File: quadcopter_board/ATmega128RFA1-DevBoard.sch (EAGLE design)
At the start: 75 parts, among them J1 ISP, Q1 CJ2302, Q2 CJ2302, Q3 CJ2302, Q4 CJ2302, U1 ATMEGA128RFA1

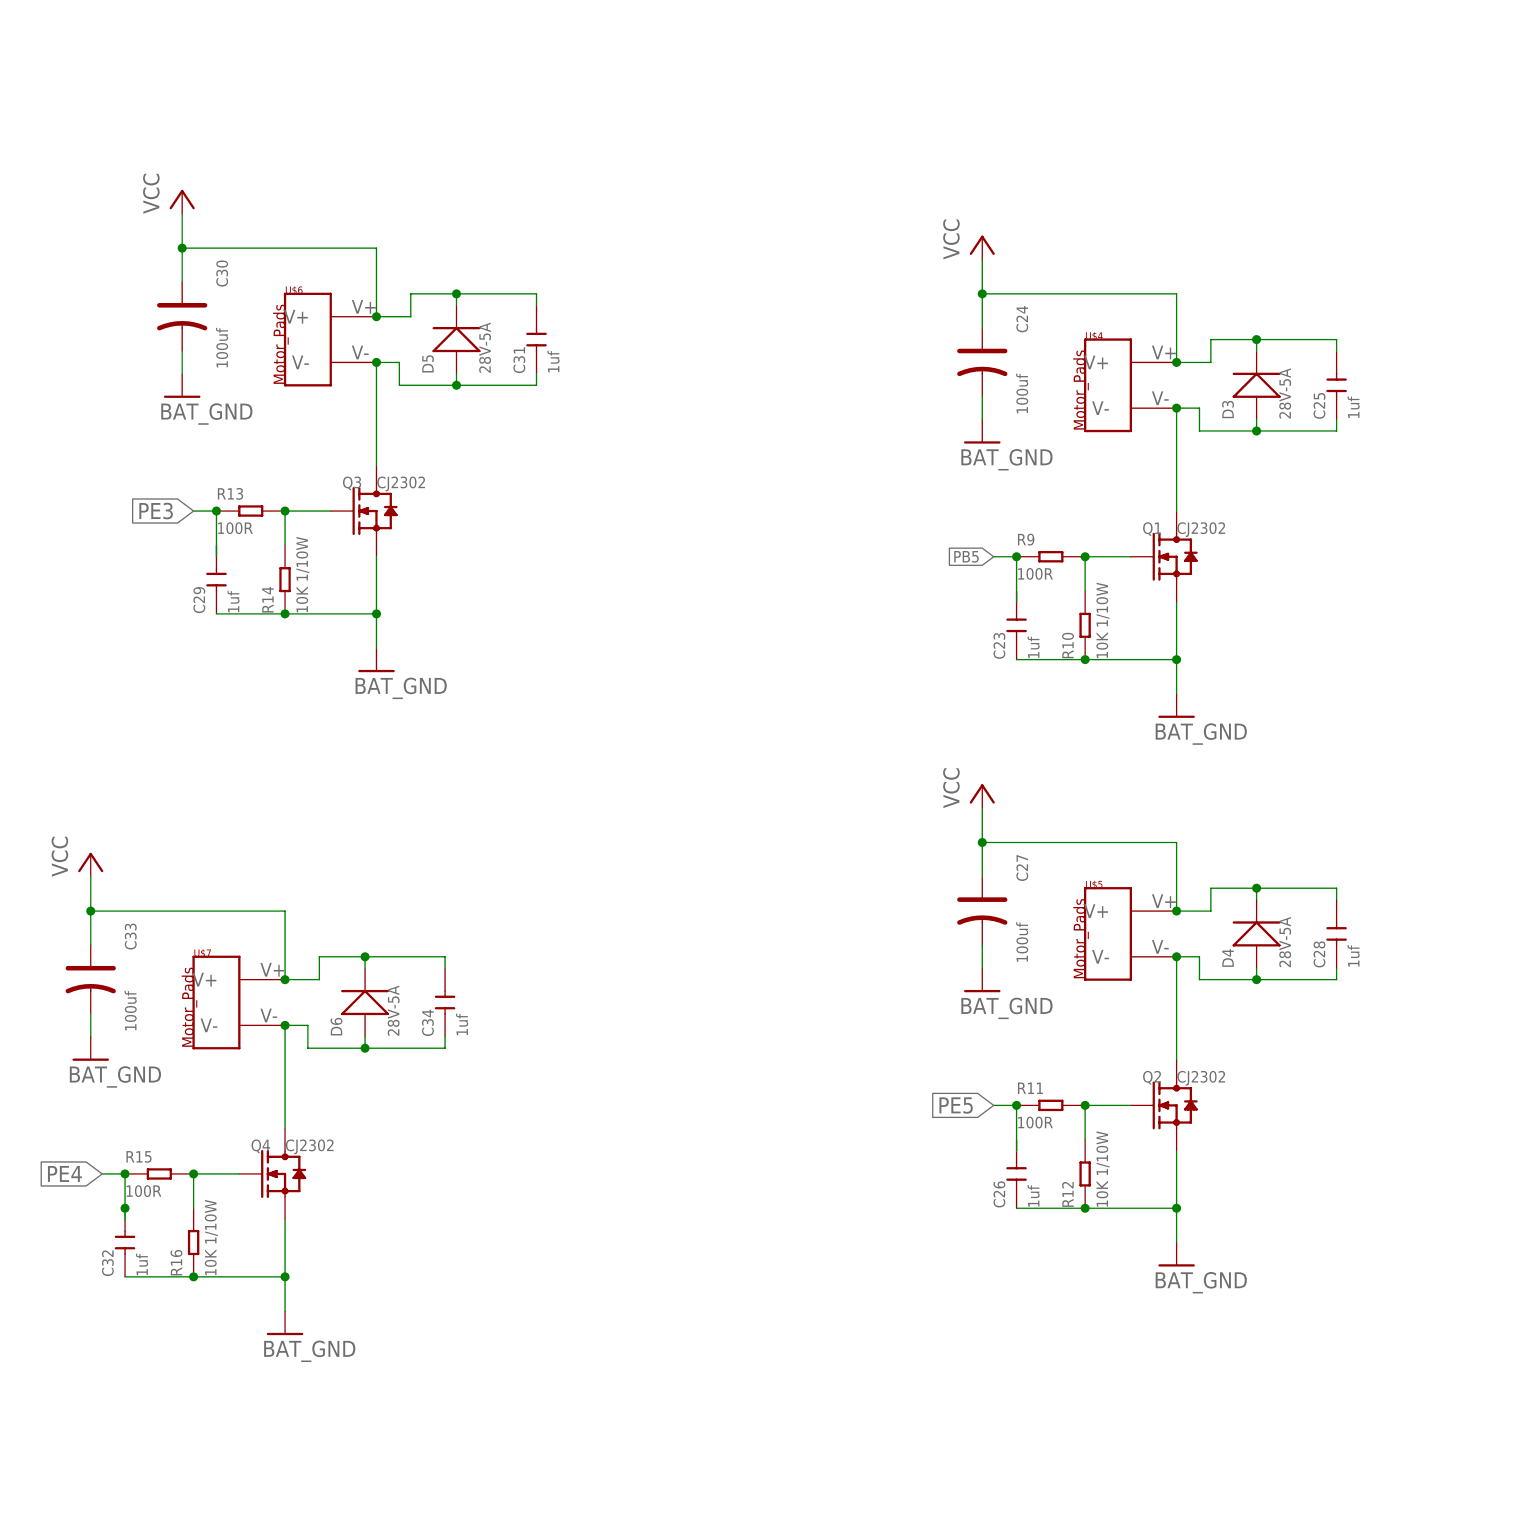
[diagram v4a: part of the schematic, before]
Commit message: clear up of motor driver layout
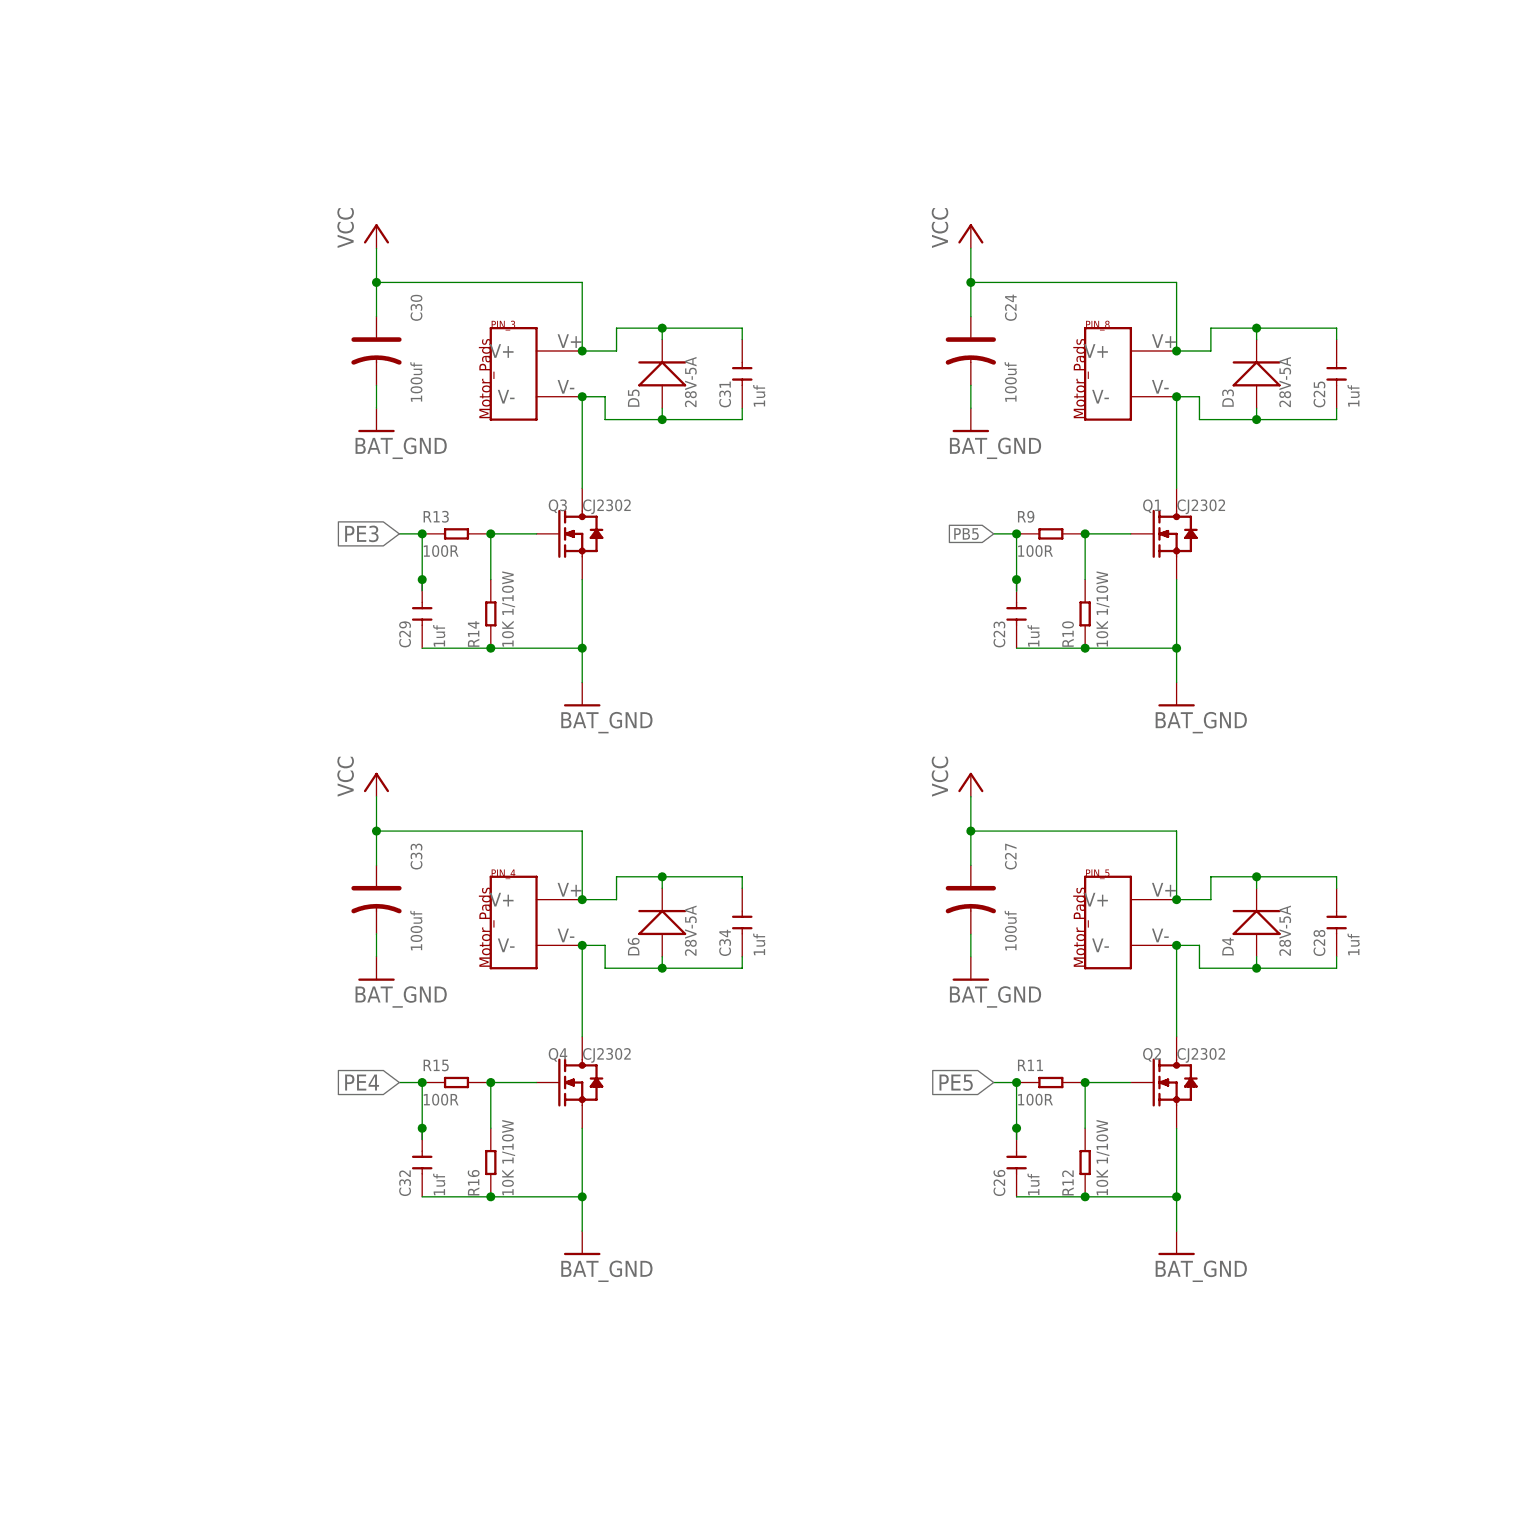
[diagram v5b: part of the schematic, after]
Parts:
- removed U$4, U$5, U$6, U$7: MOTOR_PADS, Andranik-Lab4:MOTOR_PADS
- added PIN_3, PIN_4, PIN_5, PIN_8: MOTOR_PADS, Andranik-Lab4:MOTOR_PADS
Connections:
- net N$19: now also PIN_8.V-; no longer U$4.V-
- net N$22: now also PIN_5.V-; no longer U$5.V-
- net N$25: now also PIN_3.V-; no longer U$6.V-
- net N$28: now also PIN_4.V-; no longer U$7.V-
- net PB5: now also C23.2
- net PE3: now also C29.2
- net PE5: now also C26.2
- net VCC: now also PIN_3.V+, PIN_4.V+, PIN_5.V+, PIN_8.V+; no longer U$4.V+, U$5.V+, U$6.V+, U$7.V+
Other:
- moved on the sheet: C23, C24, C25, C26, C27, C28, C29, C30, C31, C32, C33, C34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

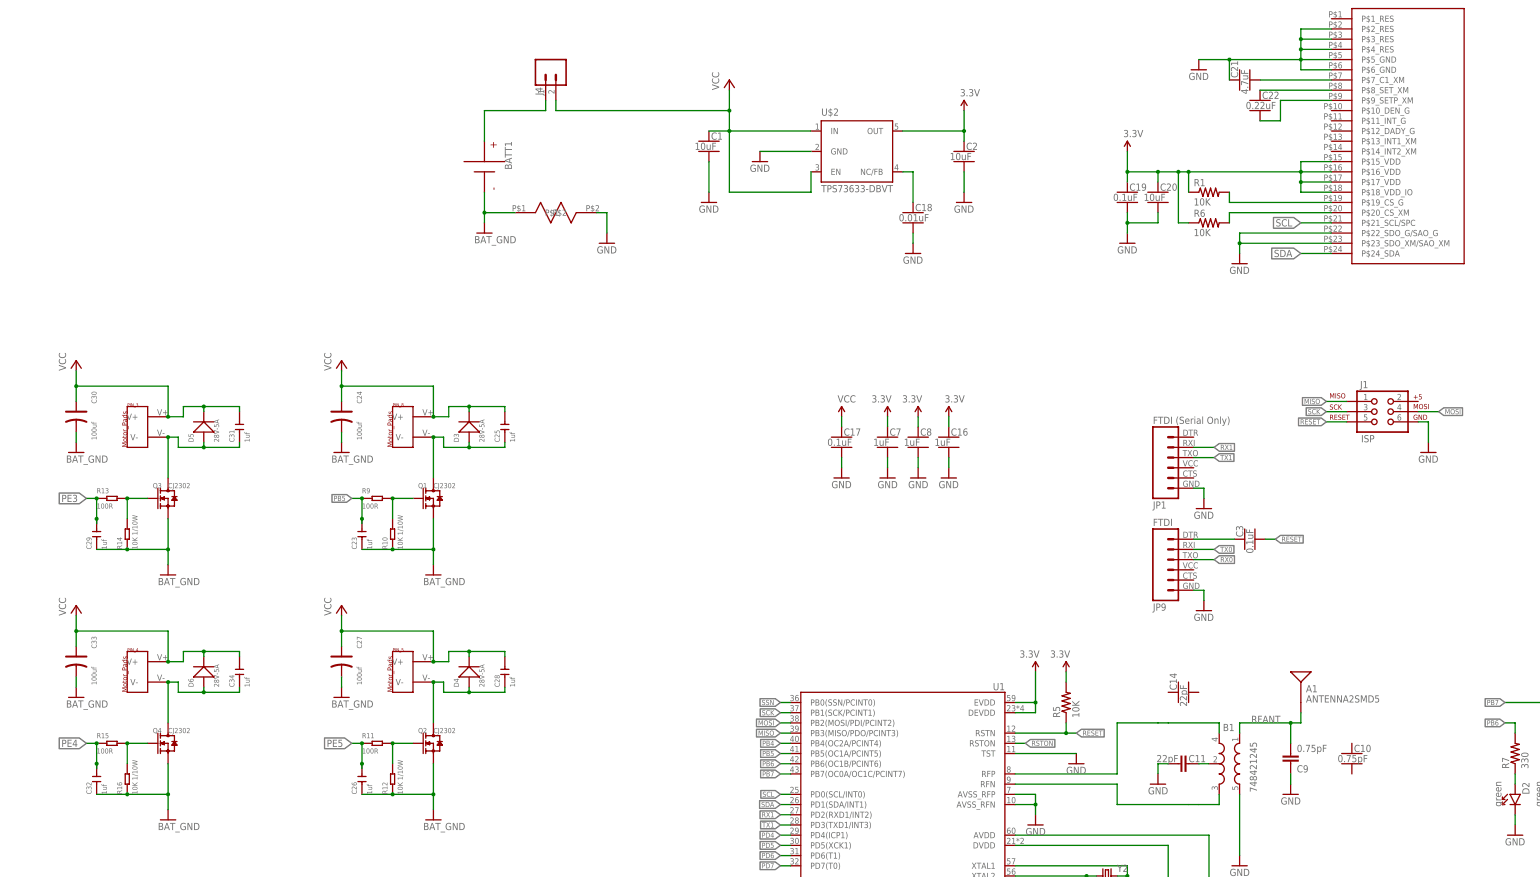
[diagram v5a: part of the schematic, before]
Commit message: changed component on motor driver
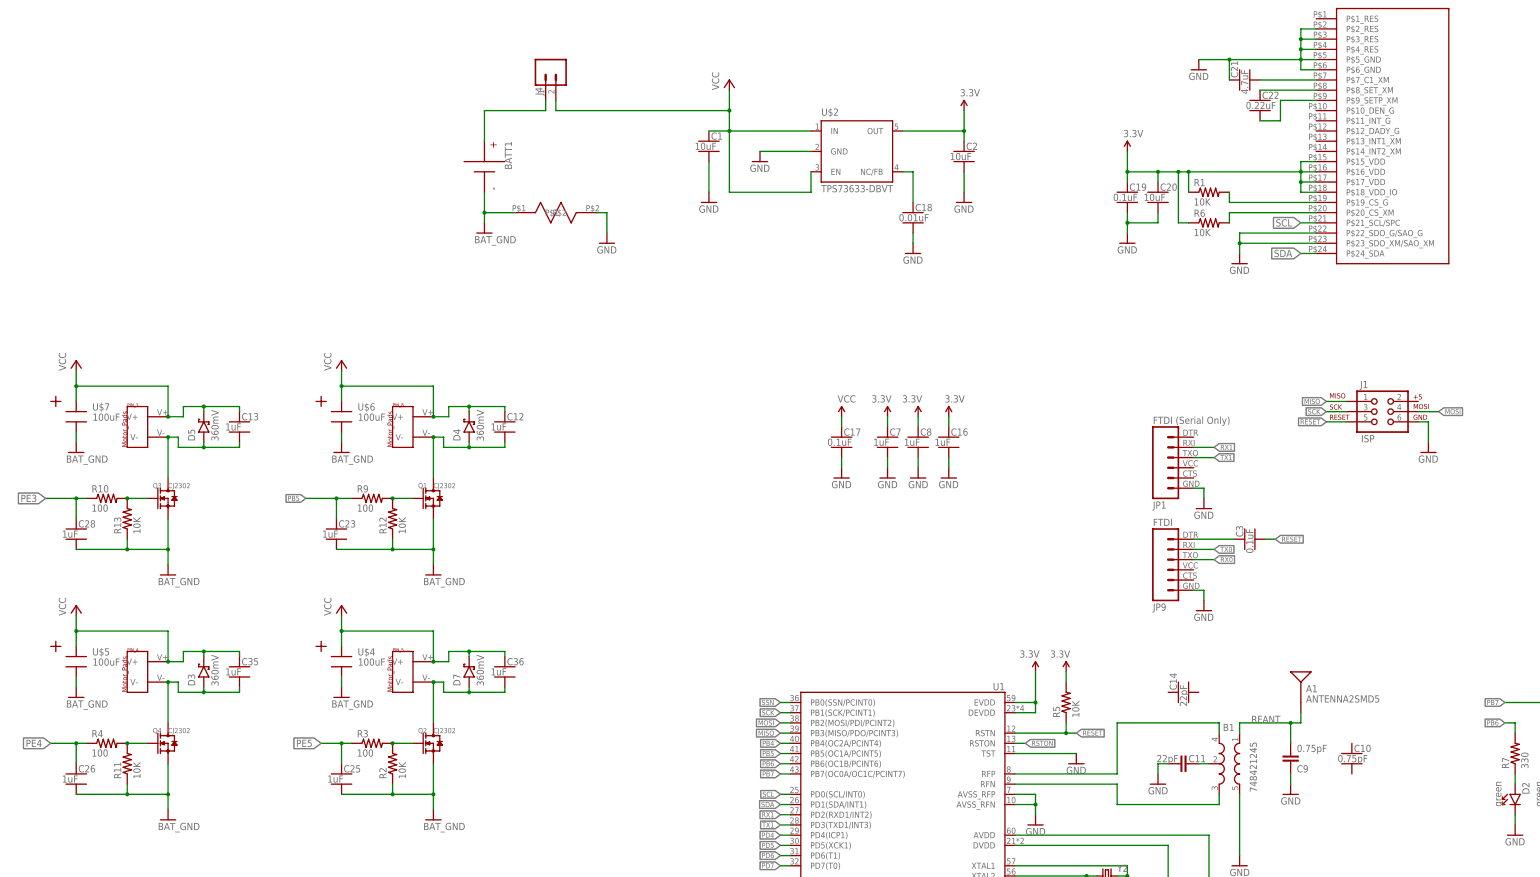
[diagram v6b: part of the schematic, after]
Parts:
- removed C24, C27, C30, C33: 100uf, Seeed-Capacitor-2016:TANTALUM-SMD-100UF-10V(AVX-B)
- removed C29, C32: 1uf, Seeed-Capacitor-2016:CERAMIC-1UF-10V-10%-X5R(0402)
- removed C31, C34: 1uf, Seeed-Capacitor-2016:CERAMIC-1UF-25V-10%-X7R(0603)
- removed D6: 28V-5A, Seeed-Diode-2016:SMD-DIODE-SCHOTTKY-28V-5A(DO-214AA)
- removed R14, R16: 10K 1/10W, Seeed-Resistor-2016:SMD-RES-10K-5%-1/10W(0603)
- removed R15: 100R, Seeed-Resistor-2016:SMD-RES-100R-5%-1/10W(0603)
- added C12, C13, C35, C36: 1uF, quadparts_prebuilt:CAPACITOR-NP_SMD-2012-0805_CERAMIC-1UF
- added D7: 360mV, quadparts_prebuilt:DIODE-SCHOTTKY_SMD-SOD123-360MV
- added R2: 10K, quadparts_prebuilt:RESISTOR_SMD-2012-0805-10K
- added R3, R4: 100, quadparts_prebuilt:RESISTOR_SMD-2012-0805-100
- added U$4, U$5, U$6, U$7: 100uF, quadparts:POLAR_CAP
- C23, C26: value 1uf -> 1uF; device Seeed-Capacitor-2016:CERAMIC-1UF-10V-10%-X5R(0402) -> quadparts_prebuilt:CAPACITOR-NP_SMD-2012-0805_CERAMIC-1UF
- C25, C28: value 1uf -> 1uF; device Seeed-Capacitor-2016:CERAMIC-1UF-25V-10%-X7R(0603) -> quadparts_prebuilt:CAPACITOR-NP_SMD-2012-0805_CERAMIC-1UF
- D3, D4, D5: value 28V-5A -> 360mV; device Seeed-Diode-2016:SMD-DIODE-SCHOTTKY-28V-5A(DO-214AA) -> quadparts_prebuilt:DIODE-SCHOTTKY_SMD-SOD123-360MV
- R10: value 10K 1/10W -> 100; device Seeed-Resistor-2016:SMD-RES-10K-5%-1/10W(0603) -> quadparts_prebuilt:RESISTOR_SMD-2012-0805-100
- R11, R13: value 100R -> 10K; device Seeed-Resistor-2016:SMD-RES-100R-5%-1/10W(0603) -> quadparts_prebuilt:RESISTOR_SMD-2012-0805-10K
- R12: value 10K 1/10W -> 10K; device Seeed-Resistor-2016:SMD-RES-10K-5%-1/10W(0603) -> quadparts_prebuilt:RESISTOR_SMD-2012-0805-10K
- R9: value 100R -> 100; device Seeed-Resistor-2016:SMD-RES-100R-5%-1/10W(0603) -> quadparts_prebuilt:RESISTOR_SMD-2012-0805-100
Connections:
- net BAT_GND: now also C23.2, C25.2, C26.2, C28.2, R11.1, R13.1, R2.1, U$4.2, U$5.2, U$6.2, U$7.2; no longer C23.1, C24.-, C26.1, C27.-, C29.1, C30.-, C32.1, C33.-, R10.1, R14.1, R16.1
- net N$18: now also R12.2; no longer R10.2
- net N$19: now also C12.2, D4.A; no longer C25.1, D3.+
- net N$21: now also R2.2, R3.2; no longer R11.2, R12.2
- net N$22: now also C36.2, D7.A; no longer C28.1, D4.+
- net N$24: now also R10.2; no longer R14.2
- net N$25: now also C13.2, D5.A; no longer C31.1, D5.+
- net N$27: now also R11.2, R4.2; no longer R15.2, R16.2
- net N$28: now also C35.2, D3.A; no longer C34.1, D6.+
- net PB5: now also C23.1; no longer C23.2
- net PE3: now also C28.1, R10.1; no longer C29.2, R13.1
- net PE4: now also C26.1, R4.1; no longer C32.2, R15.1
- net PE5: now also C25.1, R3.1; no longer C26.2, R11.1
- net VCC: now also C12.1, C13.1, C35.1, C36.1, D3.C, D4.C, D5.C, D7.C, U$4.1, U$5.1, U$6.1, U$7.1; no longer C24.+, C25.2, C27.+, C28.2, C30.+, C31.2, C33.+, C34.2, D3.-, D4.-, D5.-, D6.-
